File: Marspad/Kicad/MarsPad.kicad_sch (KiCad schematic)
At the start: 30 parts, among them J1 OLED_128x64, SW1 RotaryEncoder_Switch, SW2 RotaryEncoder_Switch, U2 RP2040_Zero

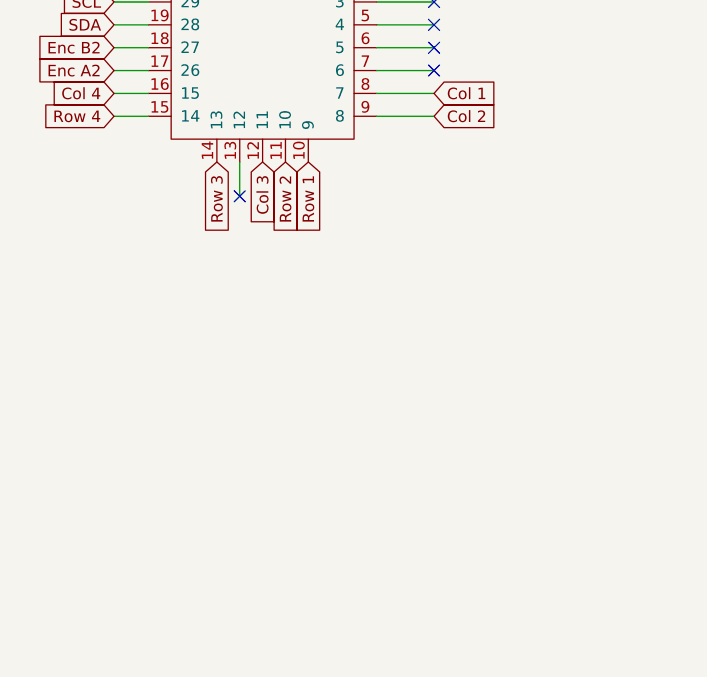
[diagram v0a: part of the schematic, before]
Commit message: added header for WS2812 led strips
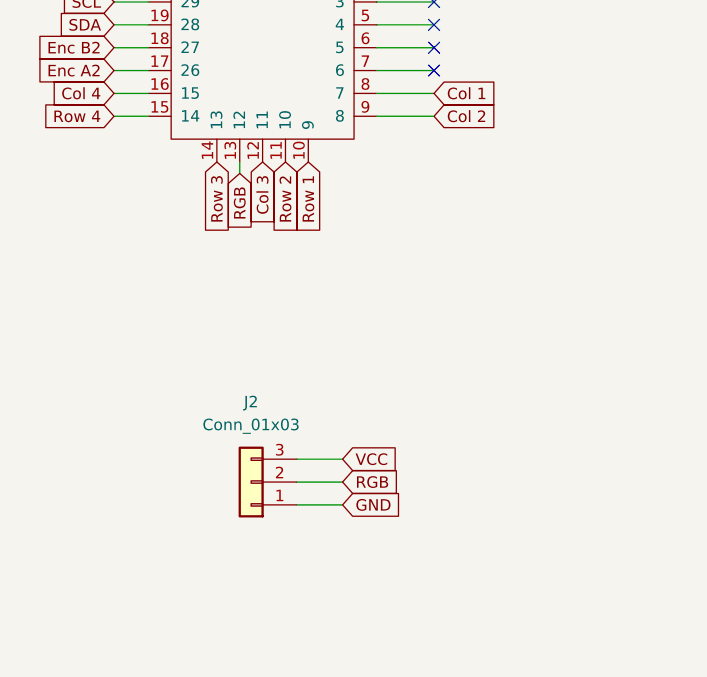
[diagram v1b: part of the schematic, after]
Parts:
- added J2: Conn_01x03, Connector_PinSocket_2.54mm:PinSocket_1x03_P2.54mm_Vertical, symbol Connector_Generic:Conn_01x03
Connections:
- net GND: now also J2.1 (Pin_1)
- net VCC: now also J2.3 (Pin_3)
- net RGB: now reaches U2.13 (12)
- net RGB: now also J2.2 (Pin_2)
- no-connect marks 7 -> 6
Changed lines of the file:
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@@
-	)
-	(no_connect
-		(at 46.99 99.06)
 	)
 	(no_connect
@@
 	(wire
 		(pts
+			(xy 53.34 133.35) (xy 58.42 133.35)
+		)
+		(stroke
+			(width 0)
+			(type default)
+		)
+	)
+	(wire
+		(pts
 			(xy 229.87 97.79) (xy 229.87 121.92)
 		)
@@
 	(wire
 		(pts
+			(xy 53.34 130.81) (xy 58.42 130.81)
+		)
+		(stroke
+			(width 0)
+			(type default)
+		)
+	)
+	(wire
+		(pts
 			(xy 199.39 140.97) (xy 199.39 121.92)
 		)
@@
 	(wire
 		(pts
+			(xy 46.99 95.25) (xy 46.99 96.52)
+		)
+		(stroke
+			(width 0)
+			(type default)
+		)
+	)
+	(wire
+		(pts
 			(xy 62.23 72.39) (xy 68.58 72.39)
 		)
@@
 	(wire
 		(pts
-			(xy 46.99 95.25) (xy 46.99 99.06)
+			(xy 53.34 128.27) (xy 58.42 128.27)
 		)
 		(stroke
@@
 	(global_label "VCC"
 		(shape input)
+		(at 58.42 128.27 0)
+		(fields_autoplaced yes)
+		(effects
+			(font
+				(size 1.27 1.27)
+			)
+			(justify left)
+		)
+		(property "Intersheetrefs" "${INTERSHEET_REFS}"
+			(at 65.0338 128.27 0)
+			(effects
+				(font
+					(size 1.27 1.27)
+				)
+				(justify left)
+				(hide yes)
+			)
+		)
+	)
+	(global_label "VCC"
+		(shape input)
 		(at 60.96 35.56 90)
 		(fields_autoplaced yes)
@@
 		)
 	)
+	(global_label "GND"
+		(shape input)
+		(at 58.42 133.35 0)
+		(fields_autoplaced yes)
+		(effects
+			(font
+				(size 1.27 1.27)
+			)
+			(justify left)
+		)
+		(property "Intersheetrefs" "${INTERSHEET_REFS}"
+			(at 65.2757 133.35 0)
+			(effects
+				(font
+					(size 1.27 1.27)
+				)
+				(justify left)
+				(hide yes)
+			)
+		)
+	)
 	(global_label "SDA"
 		(shape input)
@@
 		)
 	)
+	(global_label "RGB"
+		(shape input)
+		(at 58.42 130.81 0)
+		(fields_autoplaced yes)
+		(effects
+			(font
+				(size 1.27 1.27)
+			)
+			(justify left)
+		)
+		(property "Intersheetrefs" "${INTERSHEET_REFS}"
+			(at 65.2152 130.81 0)
+			(effects
+				(font
+					(size 1.27 1.27)
+				)
+				(justify left)
+				(hide yes)
+			)
+		)
+	)
 	(global_label "Row 1"
 		(shape input)
@@
 		(property "Intersheetrefs" "${INTERSHEET_REFS}"
 			(at 44.45 104.1618 90)
+			(effects
+				(font
+					(size 1.27 1.27)
+				)
+				(justify right)
+				(hide yes)
+			)
+		)
+	)
+	(global_label "RGB"
+		(shape input)
+		(at 46.99 96.52 270)
+		(fields_autoplaced yes)
+		(effects
+			(font
+				(size 1.27 1.27)
+			)
+			(justify right)
+		)
+		(property "Intersheetrefs" "${INTERSHEET_REFS}"
+			(at 46.99 103.3152 90)
 			(effects
 				(font
@@
 					(unit 1)
 				)
+			)
+		)
+	)
+	(symbol
+		(lib_id "Connector_Generic:Conn_01x03")
+		(at 48.26 130.81 180)
+		(unit 1)
+		(exclude_from_sim no)
+		(in_bom yes)
+		(on_board yes)
+		(dnp no)
+		(fields_autoplaced yes)
+		(property "Reference" "J2"
+			(at 48.26 121.92 0)
+			(effects
+				(font
+					(size 1.27 1.27)
+				)
+			)
+		)
+		(property "Value" "Conn_01x03"
+			(at 48.26 124.46 0)
+			(effects
+				(font
+					(size 1.27 1.27)
+				)
+			)
+		)
+		(property "Footprint" "Connector_PinSocket_2.54mm:PinSocket_1x03_P2.54mm_Vertical"
+			(at 48.26 130.81 0)
+			(effects
+				(font
+					(size 1.27 1.27)
+				)
+				(hide yes)
+			)
+		)
+		(property "Datasheet" "~"
+			(at 48.26 130.81 0)
+			(effects
+				(font
+					(size 1.27 1.27)
+				)
+				(hide yes)
+			)
+		)
+		(property "Description" "Generic connector, single row, 01x03, script generated (kicad-library-utils/schlib/autogen/connector/)"
+			(at 48.26 130.81 0)
+			(effects
+				(font
+					(size 1.27 1.27)
+				)
+				(hide yes)
+			)
+		)
+		(pin "1"
+		)
+		(pin "3"
+		)
+		(pin "2"
+		)
+		(instances
+			(project ""
+				(path "/fd71ca4a-34f4-461e-83c4-fa47b2aa2afa"
+					(reference "J2")
+					(unit 1)
+				)

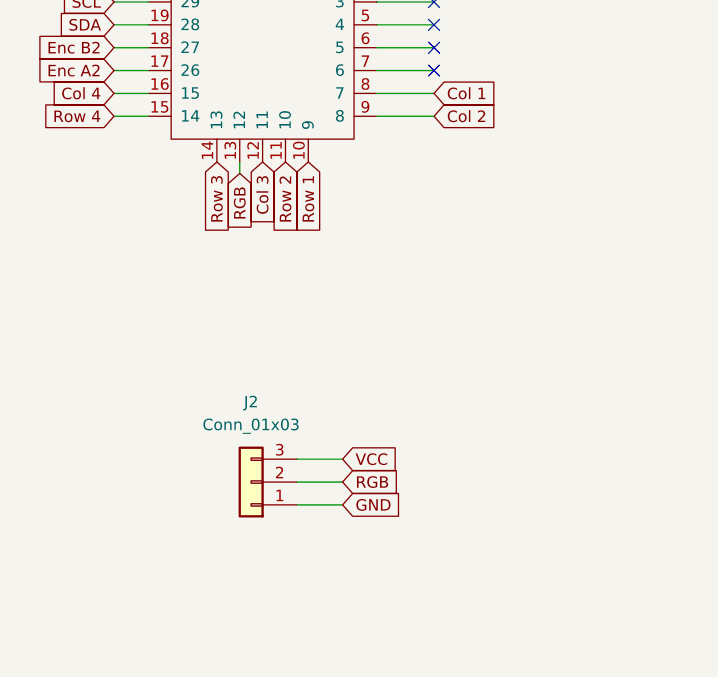
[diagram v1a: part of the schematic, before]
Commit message: added RGB headers for WS2812 LEDs and fixed other artifacts.
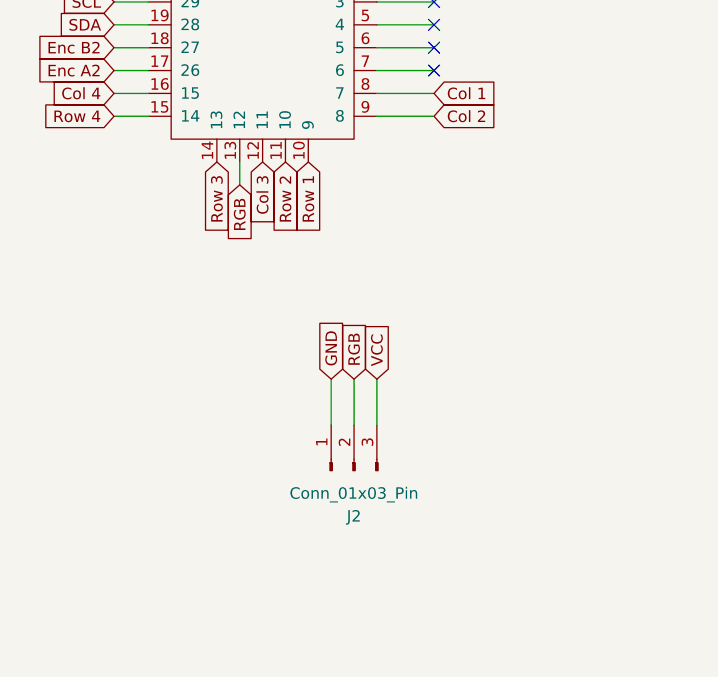
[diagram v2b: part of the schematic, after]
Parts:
- removed J2: Conn_01x03, Connector_PinSocket_2.54mm:PinSocket_1x03_P2.54mm_Vertical, symbol Connector_Generic:Conn_01x03
- added J2: Conn_01x03_Pin, Connector_PinSocket_2.54mm:PinSocket_1x03_P2.54mm_Vertical, symbol Connector:Conn_01x03_Pin
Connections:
- net GND: now also J2.1 (Pin_1)
- net RGB: now also J2.2 (Pin_2)
- net VCC: now also J2.3 (Pin_3)
